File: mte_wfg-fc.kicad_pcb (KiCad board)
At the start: 2 copper layers, 200 x 75 mm, 396 parts, among them J101 MOLEX_KK-254, J102 CONN_COAXIAL, J103 CONN_COAXIAL, J104 Conn_02x10_Odd_Even, J105 Conn_01x10, J106 Conn_01x10, J107 CONN_COAXIAL, J108 CONN_COAXIAL, J601 Conn_01x03, J602 Conn_01x04, J801 Conn_01x03, Q501 BSS315P, Q502 BSS316N, Q701 IRF7241, Q702 BSS84, Q703 BSS138, Q704 IRF7468, Q705 BSS138, Q706 IRF7468, Q707 IRF7241, Q708 BSS84, Q709 BC847, Q710 BC857, Q711 BC847, Q712 BC857, Q713 BSS138, Q714 BSS138, Q715 IRF7241, Q801 BSS138, Q802 BSS138, Q803 BSS84, Q804 BSS138, Q805 BSS138, Q806 BSS138, U201 LT1819, U202 74LVC1G157, U203 AD8065, U204 AD8065, U205 74LVC2G14, U206 74LVC2G14, U207 AD8611, U208 74LVC1G157, U209 74LVC1T45, U210 AD8611, U211 74LVC273, U212 74LVC1T45, U213 74LVC273, U301 AD9834, U302 MCP41050, U401 AD5721, U402 AD5721, U403 LMH6503, U404 TLV271, U405 MCP9700T-E/TT, U406 LM4132-2, U407 MCP41050, U408 LT1363, U409 MCP41050, U410 LMH6321, U411 TLV271, U501 TLV271, U502 TLV1117-ADJ, U503 74LVC1T45, U504 MCP9700T-E/TT, U601 74LVC1G157, U602 STM32F101RCTx, U603 74HC138, U604 24LC04, U701 LM4132-3.3, U702 STM809T, U703 NCP5661DT33, U801 SN65MLVD203, U802 SN65LVDS2, U803 SN65MLVD200A, U804 PCF8574, U805 74LVC1G157, X201 FOX924B-10.000, X301 CFPS-73, Y601 16MHz

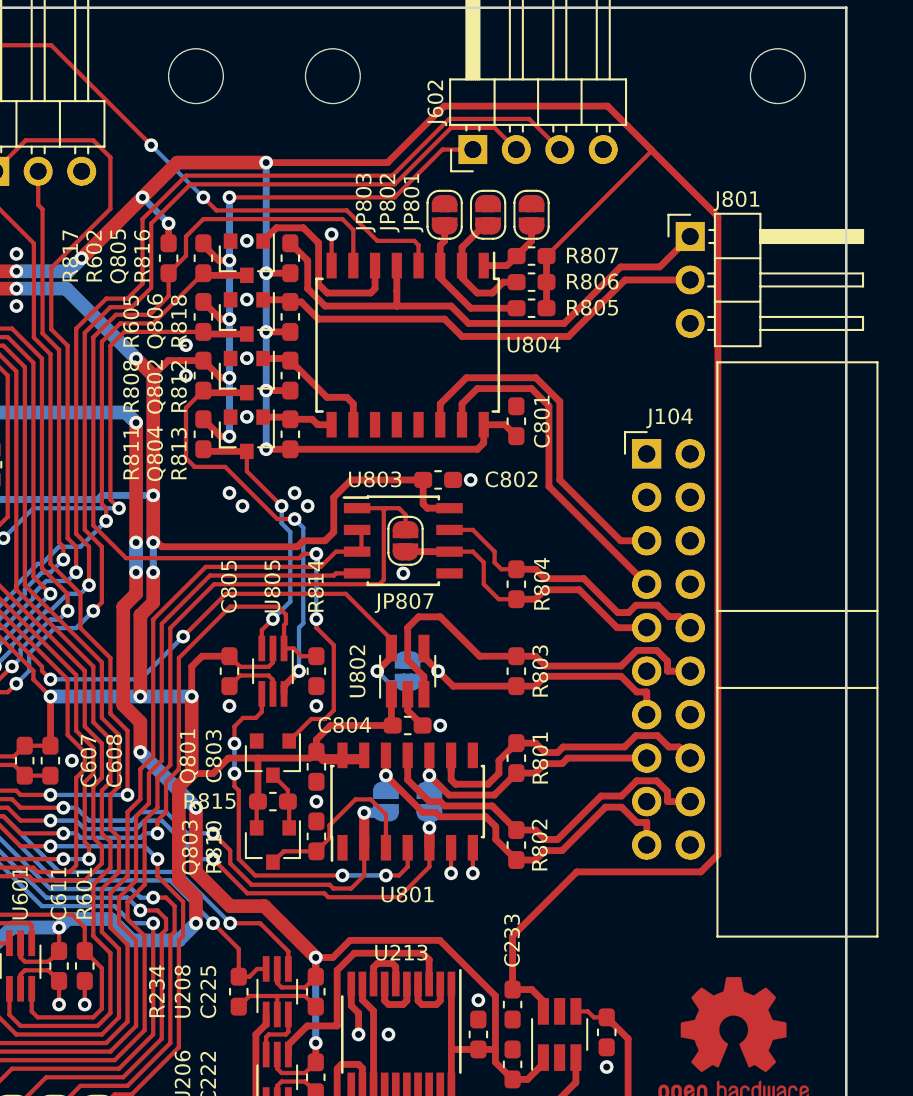
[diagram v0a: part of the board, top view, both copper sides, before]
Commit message: Changed boot pin control polarity, cleaned up schematic, updated PCB
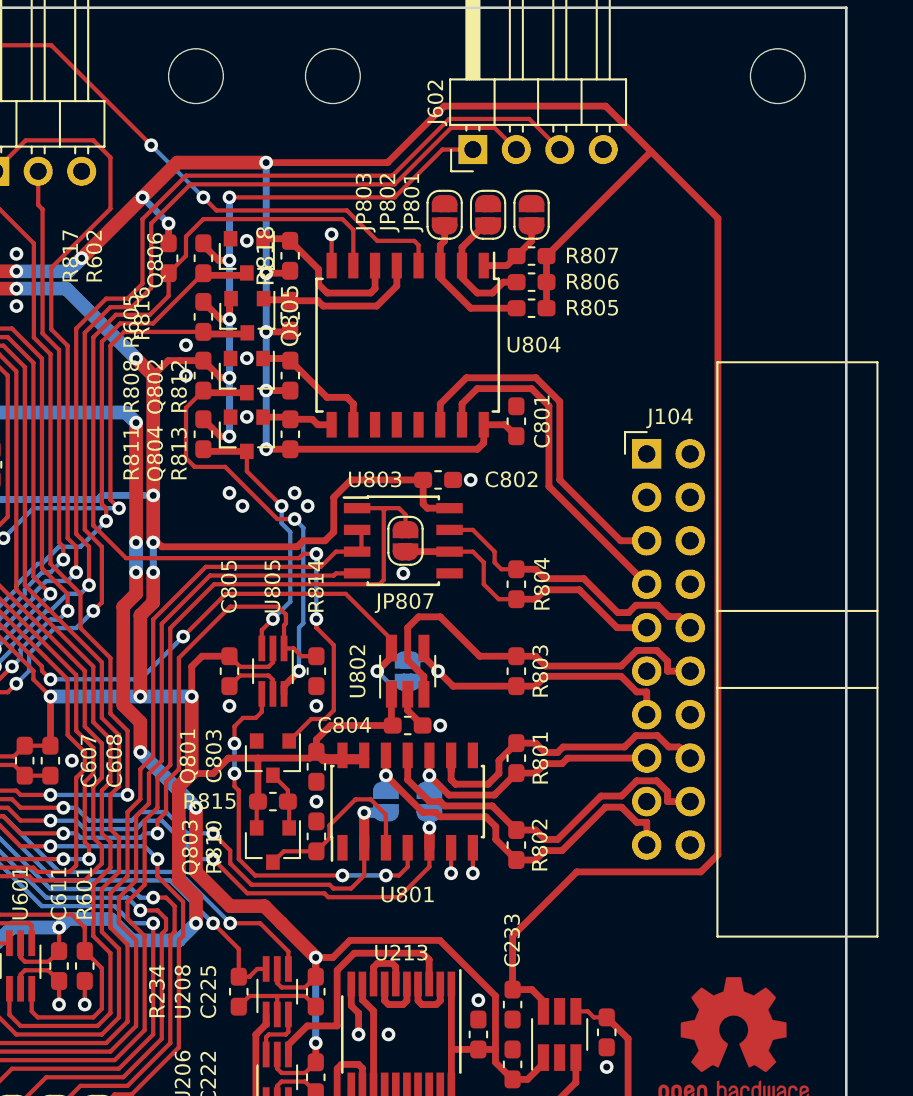
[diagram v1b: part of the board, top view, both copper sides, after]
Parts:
- removed J801: Conn_01x03, Connector_PinHeader_2.54mm:PinHeader_1x03_P2.54mm_Horizontal
- J102, J103, J107, J108: footprint MTE:TE_1-1337541-0 -> mte:TE_1-1337541-0
- Q805: value BSS138 -> BSS84
- moved R818 3.57 mm to (212.5, 57.0)
- moved Q806 3.57 mm to (210.0, 57.0)
- moved Q805 3.36 mm to (210.0, 60.5)
- moved R816 3.36 mm to (212.5, 60.5)
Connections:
- Q805 pad 2: DGND -> +3V3D
- Q805 pad 3: /Bus Interface/NRST -> /Bus Interface/BOOT0
- Q806 pad 1: Net-(J801-Pad2) -> Net-(Q806-Pad1)
- Q806 pad 3: /Bus Interface/BOOT0 -> /Bus Interface/NRST
- R816 pad 2: Net-(J801-Pad1) -> Net-(Q805-Pad1)
- R818 pad 2: Net-(J801-Pad2) -> Net-(Q806-Pad1)
- U804 pad 5: Net-(J801-Pad1) -> Net-(Q805-Pad1)
- U804 pad 6: Net-(Q805-Pad1) -> Net-(Q806-Pad1)
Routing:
- net Net-(J801-Pad1): track 30.7 -> 0.00 mm
- net Net-(J801-Pad2): track 27.0 -> 0.00 mm
- net Net-(Q806-Pad1): track 0.00 -> 9.82 mm
- net Net-(Q805-Pad1): track 11.3 -> 9.51 mm
- net +3V3D: track 376.2 -> 377.4 mm
- net DGND: vias 126 -> 125

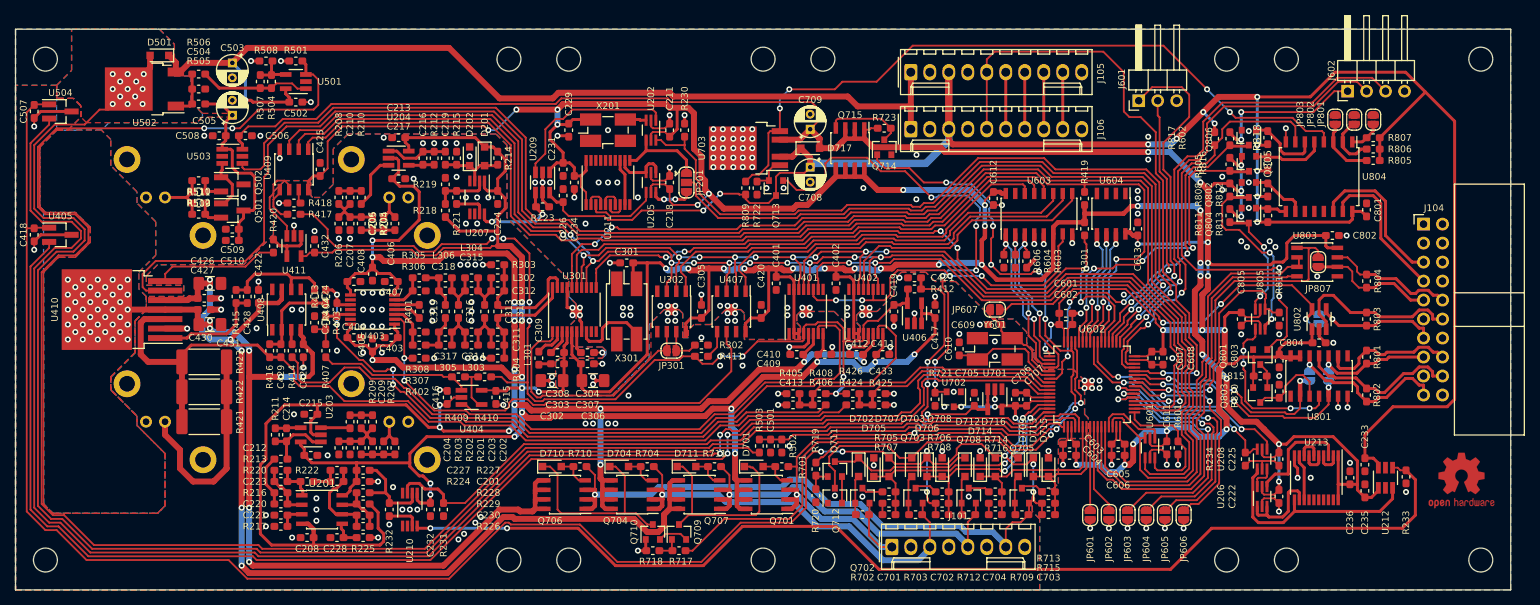
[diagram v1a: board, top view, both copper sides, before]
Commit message: Fixed reference sizes and placement
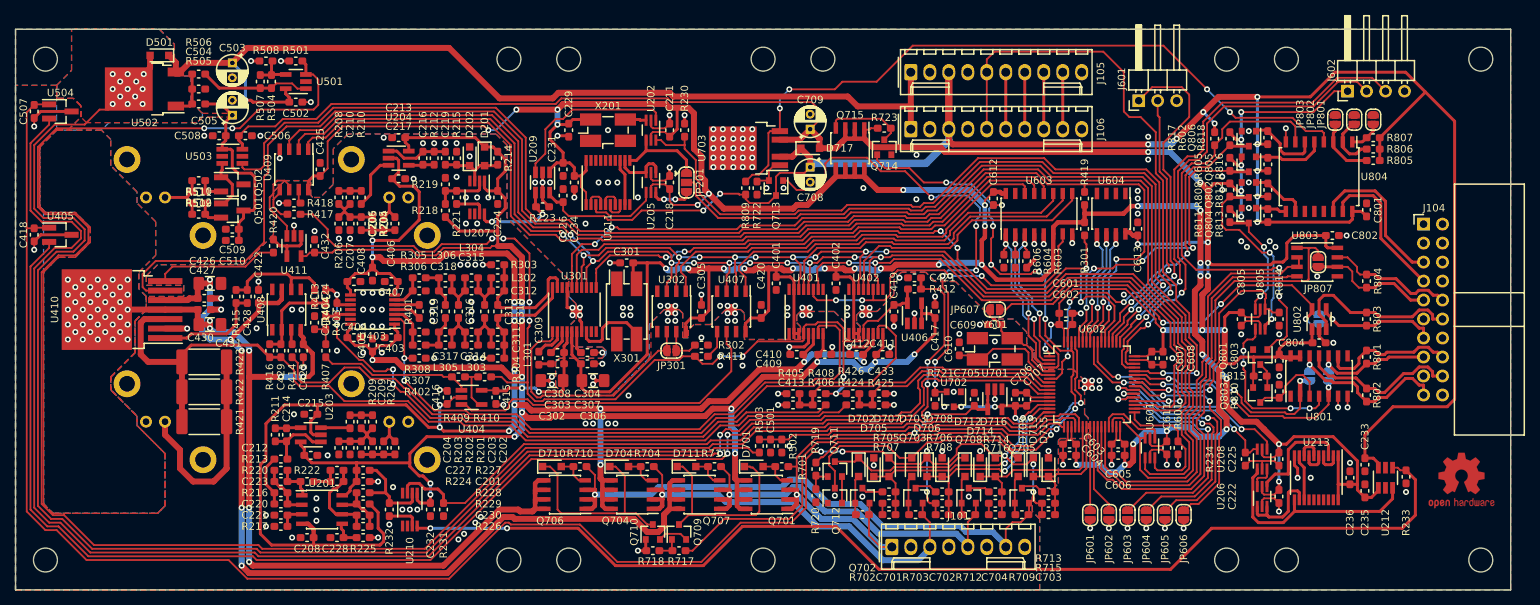
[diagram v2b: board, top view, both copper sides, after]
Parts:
- moved Q806 0.14 mm to (210.0, 57.1)
- moved Q805 0.07 mm to (210.0, 60.6)
- moved R816 0.07 mm to (212.5, 60.6)
